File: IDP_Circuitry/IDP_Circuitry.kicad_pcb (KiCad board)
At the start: 2 copper layers, 13 parts

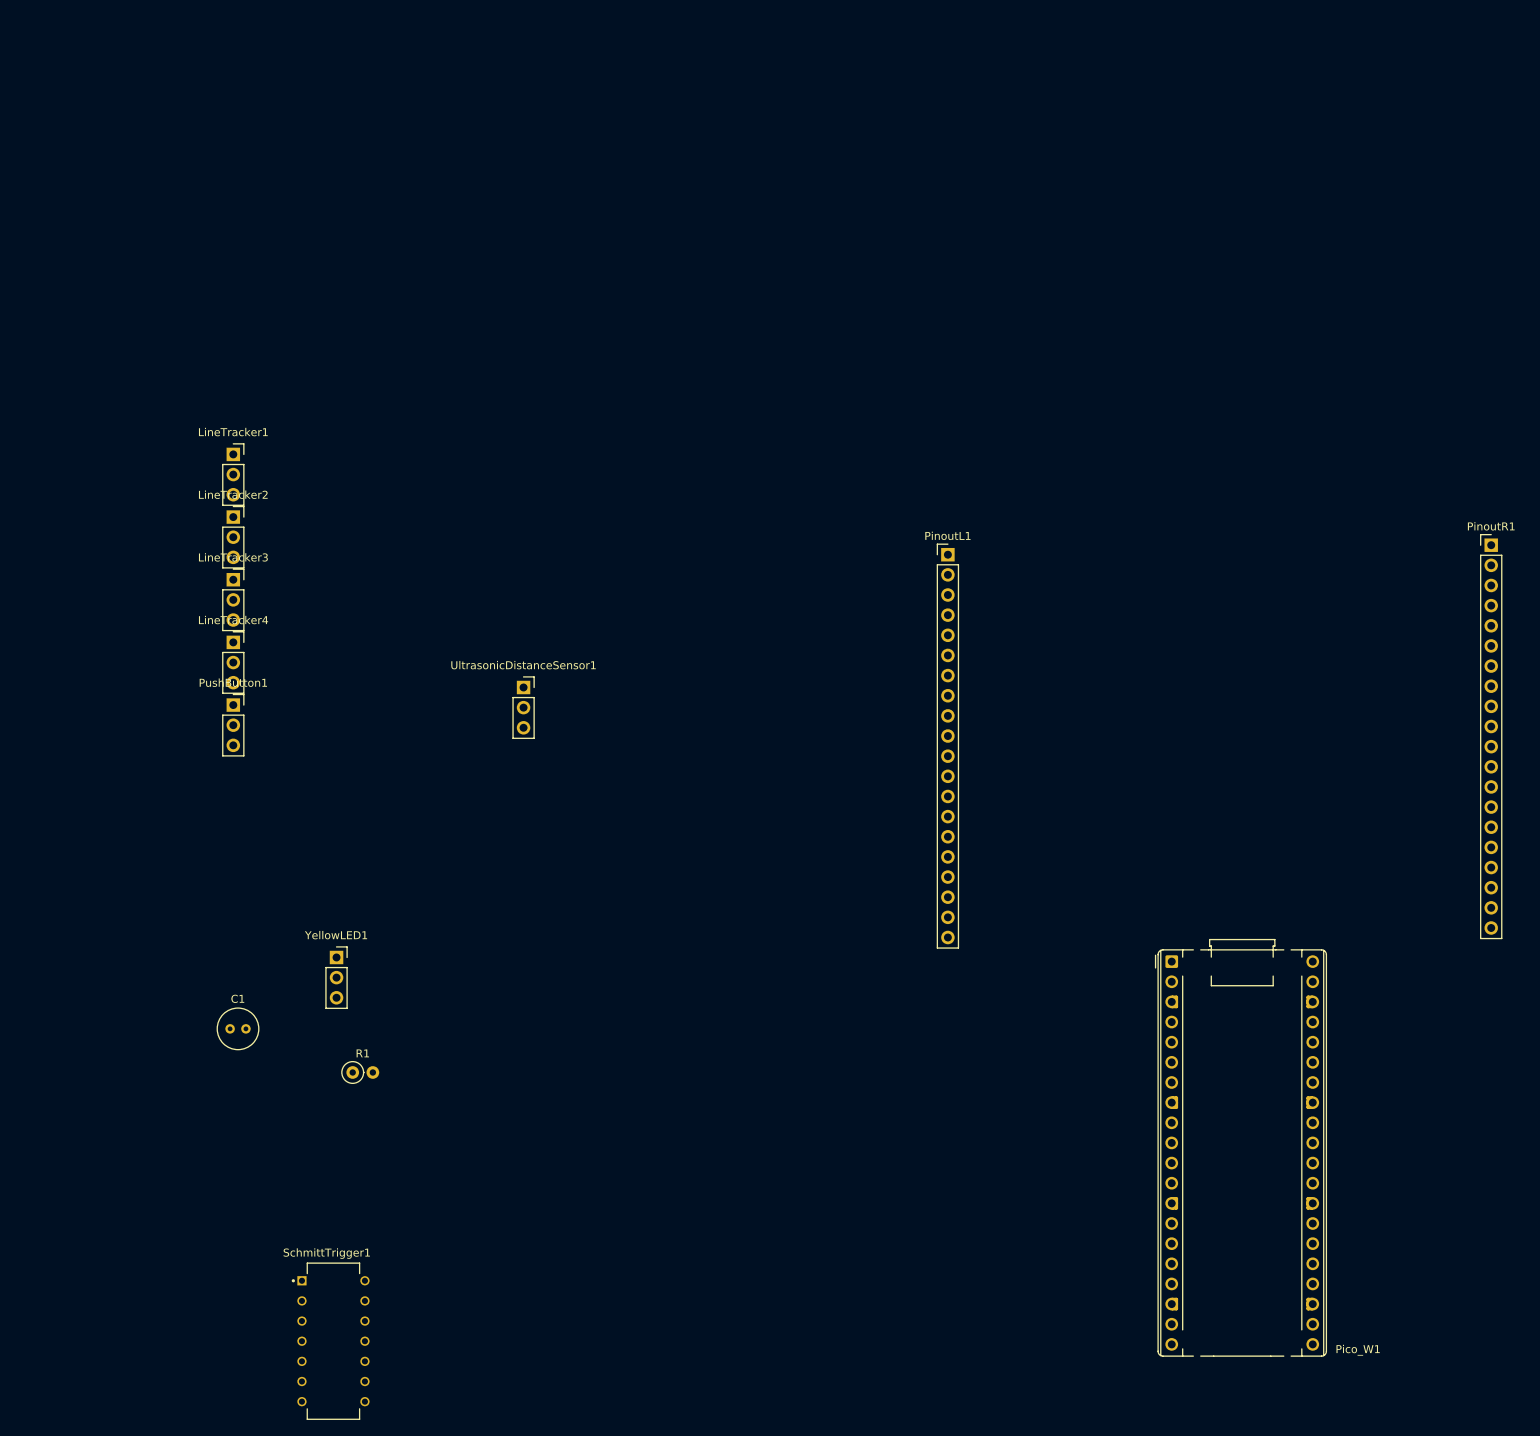
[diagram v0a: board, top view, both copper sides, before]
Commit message: updated pcb, need to change footprint to make the ic compatible with the pinout board holes
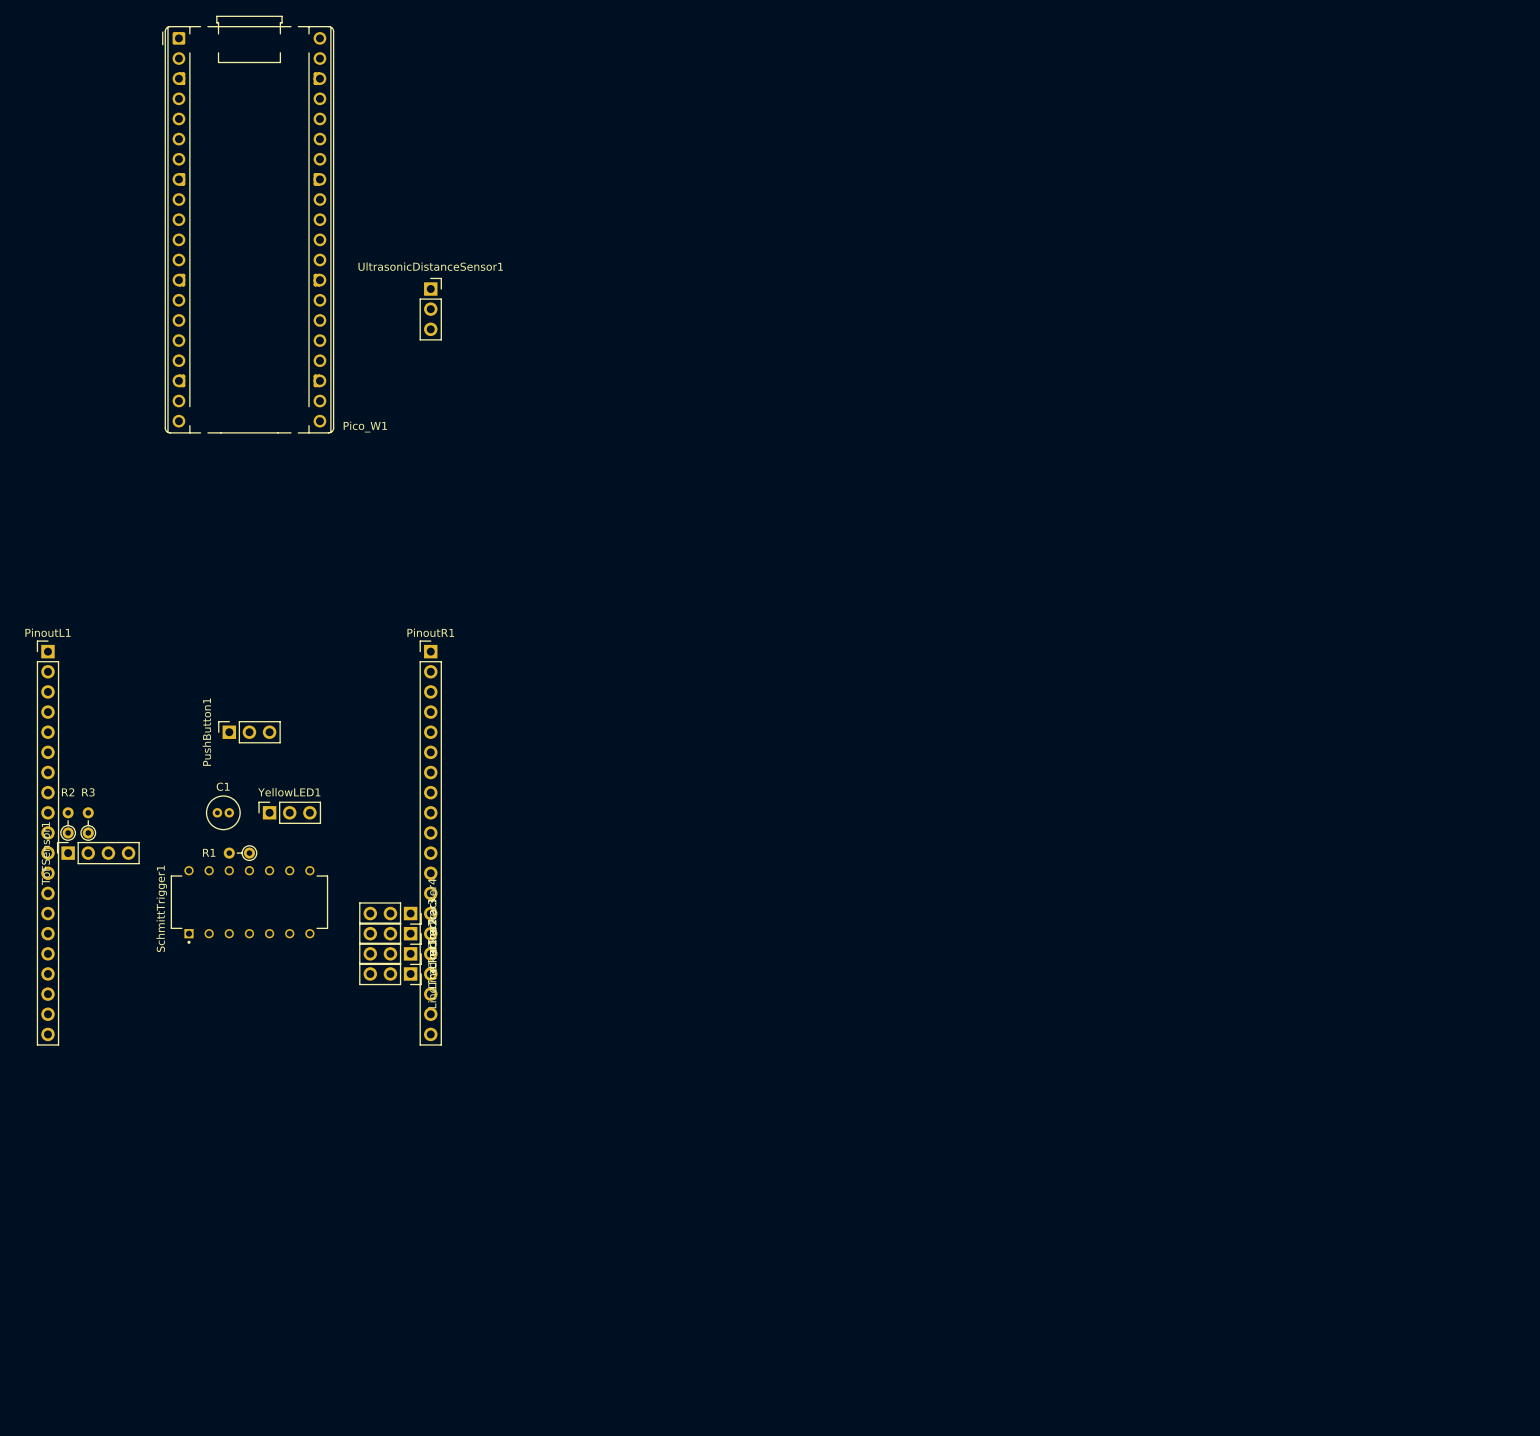
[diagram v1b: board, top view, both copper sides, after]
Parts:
- added R2: 4.7k, Resistor_THT:R_Axial_DIN0204_L3.6mm_D1.6mm_P2.54mm_Vertical, F.Cu at (5.08, 50.8)
- added R3: 4.7k, Resistor_THT:R_Axial_DIN0204_L3.6mm_D1.6mm_P2.54mm_Vertical, F.Cu at (7.62, 50.8)
- added ToFSensor1: Conn_01x04_Pin, Connector_PinSocket_2.54mm:PinSocket_1x04_P2.54mm_Vertical, F.Cu at (5.08, 53.3)
- C1: footprint Capacitor_THT:C_Radial_D5.0mm_H5.0mm_P2.00mm -> Capacitor_THT:C_Radial_D4.0mm_H5.0mm_P1.50mm
- R1: footprint Resistor_THT:R_Axial_DIN0207_L6.3mm_D2.5mm_P2.54mm_Vertical -> Resistor_THT:R_Axial_DIN0204_L3.6mm_D1.6mm_P2.54mm_Vertical
- SchmittTrigger1: footprint CD4093BE:DIP794W45P254L1969H508Q14 -> CD4093BE:CD4093BE
- moved Pico_W1 170.9 mm to (19.1, -49.4)
- moved PinoutR1 134.4 mm to (50.8, 27.9)
- moved PinoutL1 114.1 mm to (2.54, 27.9)
- moved LineTracker1 69.2 mm to (48.3, 68.6), turned to -90 degrees
- moved LineTracker2 59.4 mm to (48.3, 66.0), turned to -90 degrees
- moved SchmittTrigger1 56.4 mm to (27.9, 59.5), turned to 90 degrees
- moved UltrasonicDistanceSensor1 51.6 mm to (50.8, -17.8)
- moved LineTracker3 49.9 mm to (48.3, 63.5), turned to -90 degrees
- moved LineTracker4 40.8 mm to (48.3, 61.0), turned to -90 degrees
- moved R1 30.6 mm to (27.9, 53.3), turned to 180 degrees
- moved C1 27.3 mm to (23.9, 48.3)
- moved YellowLED1 20.1 mm to (30.5, 48.3), turned to 90 degrees
- moved PushButton1 3.46 mm to (25.4, 38.1), turned to 90 degrees
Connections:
- YellowLED1 pad 2: GND -> /3V3(OUT)
- YellowLED1 pad 3: +5V -> GND

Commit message: completed updates schematic and wired all components on the pcb. Minor tweaks likely necessary, but overall complete
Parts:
- removed Pico_W1: RaspberryPi_Pico_W, Module:RaspberryPi_Pico_Common_THT
- removed UltrasonicDistanceSensor1: Conn_01x03_Pin, Connector_PinSocket_2.54mm:PinSocket_1x03_P2.54mm_Vertical
- added ColourSensor1: Conn_01x04_Pin, Connector_PinSocket_2.54mm:PinSocket_1x04_P2.54mm_Vertical, F.Cu at (5.08, 61.0)
- added R4: 4.7k, Resistor_THT:R_Axial_DIN0204_L3.6mm_D1.6mm_P2.54mm_Vertical, F.Cu at (7.62, 45.7)
- added R5: 4.7k, Resistor_THT:R_Axial_DIN0204_L3.6mm_D1.6mm_P2.54mm_Vertical, F.Cu at (10.2, 63.5)
- moved PushButton1 29.0 mm to (48.3, 55.9), turned to -90 degrees
- moved C1 1.50 mm to (25.4, 48.3)
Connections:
- PushButton1 pad 1: /Input -> /GPIO22
- SchmittTrigger1 pad 13: /Input -> /GPIO14
- SchmittTrigger1 pad 14: unconnected-(SchmittTrigger1-VDD-Pad14) -> /3V3(OUT)
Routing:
- net /3V3(OUT): track 0.00 -> 111.2 mm
- net GND: track 0.00 -> 70.6 mm
- net /GPIO14: track 0.00 -> 27.8 mm
- net /GPIO10: track 0.00 -> 18.8 mm
- net /GPIO9: track 0.00 -> 10.2 mm
- net /GPIO11: track 0.00 -> 10.2 mm
- net /Output: track 0.00 -> 8.35 mm
- net /Input: track 0.00 -> 7.30 mm
- net /GPIO8: track 0.00 -> 5.08 mm
- net /GPIO22: track 0.00 -> 2.54 mm
- net /GPIO21: track 0.00 -> 2.54 mm
- net /GPIO20: track 0.00 -> 2.54 mm
- net /GPIO19: track 0.00 -> 2.54 mm
- net /GPIO18: track 0.00 -> 2.54 mm

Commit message: final commit, completed schematic/pcb and fully labelled
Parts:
- SchmittTrigger1: footprint CD4093BE:CD4093BE -> CD4093BE:DIP794W45P254L1969H508Q14
- moved SchmittTrigger1 33.4 mm to (50.8, 83.8)
- moved LineTracker1 32.6 mm to (71.1, 91.8)
- moved LineTracker3 32.6 mm to (71.1, 86.7)
- moved C1 32.6 mm to (48.3, 71.4)
- moved ColourSensor1 32.6 mm to (27.9, 84.1)
- moved LineTracker2 32.6 mm to (71.1, 89.2)
- moved LineTracker4 32.6 mm to (71.1, 84.1)
- moved PinoutL1 32.6 mm to (25.4, 51.1)
- moved PinoutR1 32.6 mm to (73.7, 51.1)
- moved PushButton1 32.6 mm to (71.1, 79.1)
- moved R2 32.6 mm to (27.9, 74.0)
- moved R3 32.6 mm to (30.5, 74.0)
- moved R4 32.6 mm to (30.5, 68.9)
- moved R5 32.6 mm to (33.0, 86.7)
- moved YellowLED1 32.6 mm to (53.3, 71.4)
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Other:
- board outline added: 53.3 x 101.6 mm
- board text added: "100mmx53.5mm Perforated Board"
- board text added: "2025-03-13"
- board text added: "IDP Team 212"
- board text added: "Interface Board"
- board text added: "Pin 10: GPIO07"
- board text added: "Pin 11: GPIO08"
- board text added: "Pin 12: GPIO09"
- board text added: "Pin 13: GND"
- board text added: "Pin 14: GPIO10"
- board text added: "Pin 15: GPIO11"
- board text added: "Pin 19: GPIO14"
- board text added: "Pin 23: GND"
- board text added: "Pin 24: GPIO18"
- board text added: "Pin 25: GPIO19"
- board text added: "Pin 26: GPIO20"
- board text added: "Pin 27: GPIO21"
- board text added: "Pin 29: GPIO22"
- board text added: "Pin 36: 3V3(OUT)"
- board text added: "Pin 9: GPIO06"
